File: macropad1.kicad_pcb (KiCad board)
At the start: 2 copper layers, 119.9 x 63.5 mm, 43 parts, among them J1 Conn_01x04, SW1 SW_Reed, SW2 Rotary_Encoder_Switch, U1 ATmega32U4-AU, Y1 16Mhz

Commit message: Ready for prototyping
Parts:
- removed USB1: Molex-0548190589, random-keyboard-parts:Molex-0548190589
- added GND: MountingHole_2.2mm_M2_Pad_Via, MountingHole:MountingHole_2.2mm_M2_Pad_Via, F.Cu at (37.6, 24.1)
- added GND: MountingHole_2.2mm_M2_Pad_Via, MountingHole:MountingHole_2.2mm_M2_Pad_Via, F.Cu at (37.6, 86.4)
- added GND: MountingHole_2.2mm_M2_Pad_Via, MountingHole:MountingHole_2.2mm_M2_Pad_Via, F.Cu at (169.4, 86.4)
- added GND: MountingHole_2.2mm_M2_Pad_Via, MountingHole:MountingHole_2.2mm_M2_Pad_Via, F.Cu at (169.4, 24.1)
- added J2: USB_B_Mini, Connector_USB:USB_Mini-B_Lumberg_2486_01_Horizontal, B.Cu at (65.0, 25.4)
- moved D12 5.18 mm to (165.4, 74.3)
- moved D4 5.18 mm to (165.4, 36.2)
- moved D8 5.18 mm to (165.4, 55.3)
- moved MX12 5.18 mm to (157.5, 74.3)
- moved MX4 5.18 mm to (157.5, 36.2)
- moved MX8 5.18 mm to (157.5, 55.3)
- moved D1 5.18 mm to (108.3, 36.2)
- moved D10 5.18 mm to (127.3, 74.3)
- moved D2 5.18 mm to (127.3, 36.2)
- moved D5 5.18 mm to (108.3, 55.3)
- moved D6 5.18 mm to (127.3, 55.3)
- moved D9 5.18 mm to (108.3, 74.3)
- moved MX1 5.18 mm to (100.3, 36.2)
- moved MX10 5.18 mm to (119.4, 74.3)
- moved MX2 5.18 mm to (119.4, 36.2)
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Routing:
- net /ROW_2: track 106.1 -> 61.8 mm
- net +5V: track 125.5 -> 142.3 mm, vias 2 -> 7
- net GND: track 77.9 -> 64.2 mm, vias 0 -> 2
- net D+: track 55.5 -> 68.2 mm
- net D-: track 58.1 -> 68.7 mm
- net /ROW_1: track 90.1 -> 95.2 mm
- net /COL_0: track 54.0 -> 57.9 mm
- net /ROW_0: track 99.2 -> 102.5 mm
- net /SDA: track 35.0 -> 37.4 mm
- net /SCL: track 33.9 -> 36.3 mm
- net /COL_3: track 115.2 -> 117.4 mm
- net /COL_2: track 93.6 -> 95.9 mm
- net /COL_1: track 75.8 -> 77.9 mm
- net /ENC_S2: track 25.3 -> 26.4 mm
- net /ENC_S1: track 24.6 -> 25.7 mm
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- added copper zone on F.Cu, net (none)
- removed copper zone on F.Cu, net GND
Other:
- board size 119.9 x 63.5 mm -> 139.7 x 69.8 mm
- board text added: "I suppose it's good enough..."

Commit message: Added artwork lib and eeprom
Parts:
- added U2: 24LC512, Package_SO:TSSOP-8_4.4x3mm_P0.65mm, B.Cu at (53.8, 41.9)
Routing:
- net /ROW_2: track 61.8 -> 112.4 mm
- net GND: track 64.2 -> 82.0 mm
- net /SDA: track 37.4 -> 45.1 mm
- net /SCL: track 36.3 -> 43.8 mm
- net +5V: track 142.3 -> 139.7 mm, vias 7 -> 6
- net /COL_2: track 95.9 -> 97.6 mm, vias 0 -> 1
- net /COL_0: track 57.9 -> 57.5 mm, vias 0 -> 1
- net /COL_1: track 77.9 -> 77.8 mm, vias 0 -> 1
- net /COL_3: vias 0 -> 1
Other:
- board text added: "We all gotta start somewhere..."
- board text removed: "I suppose it's good enough..."

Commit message: Added board pics
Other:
- board text added: "JLCJLCJLCJLC"

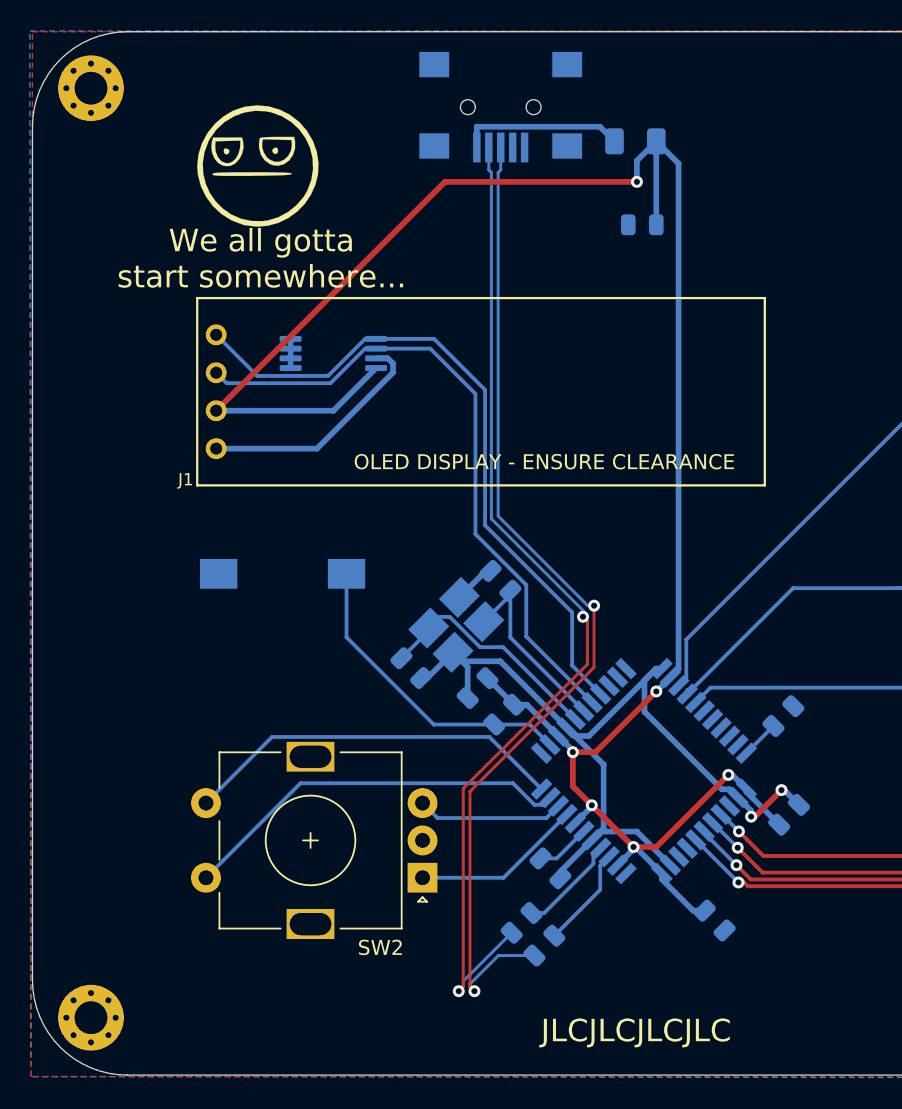
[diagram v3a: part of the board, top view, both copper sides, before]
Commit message: Fixes D+/D- swap and adds ISP header
Also moves some components around for better layout
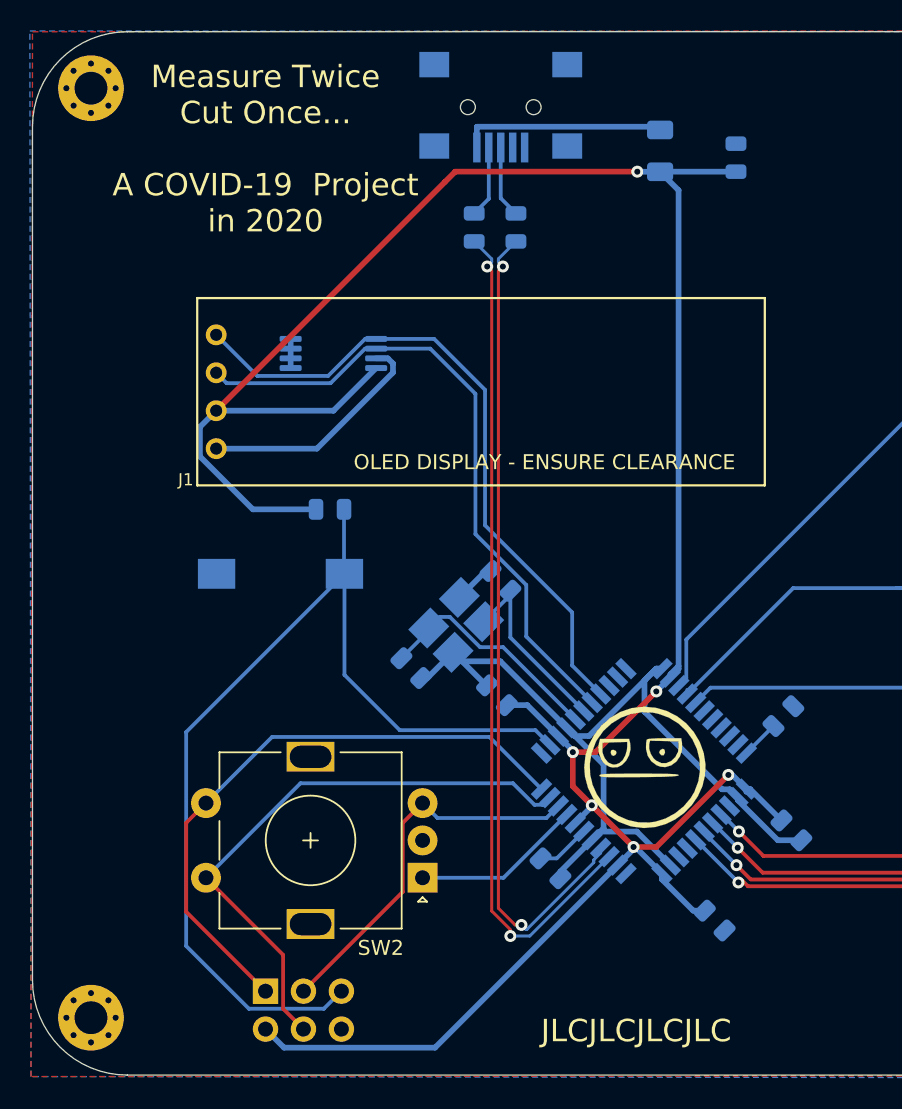
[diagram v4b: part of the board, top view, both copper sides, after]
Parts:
- removed GND (x4): MountingHole_2.2mm_M2_Pad_Via, MountingHole:MountingHole_2.2mm_M2_Pad_Via
- added J3: AVR-ISP-6, Connector_PinHeader_2.54mm:PinHeader_2x03_P2.54mm_Vertical, B.Cu at (49.3, 84.6)
- added REF**: MountingHole_2.2mm_M2_Pad_Via, MountingHole:MountingHole_2.2mm_M2_Pad_Via, F.Cu at (37.6, 86.4)
- added REF**: MountingHole_2.2mm_M2_Pad_Via, MountingHole:MountingHole_2.2mm_M2_Pad_Via, F.Cu at (169.4, 86.4)
- added REF**: MountingHole_2.2mm_M2_Pad_Via, MountingHole:MountingHole_2.2mm_M2_Pad_Via, F.Cu at (169.4, 24.1)
- added REF**: MountingHole_2.2mm_M2_Pad_Via, MountingHole:MountingHole_2.2mm_M2_Pad_Via, F.Cu at (37.6, 24.1)
- SW1: value SW_Reed -> SPST
- moved R3 48.3 mm to (63.2, 33.4), turned to 270 degrees
- moved G*** 47.9 mm to (74.7, 69.6)
- moved R2 46.6 mm to (66.0, 33.4), turned to 90 degrees
- moved R4 18.0 mm to (53.6, 52.3), turned to 0 degrees
- moved C5 7.72 mm to (80.8, 28.8), turned to 90 degrees
- moved F1 1.77 mm to (75.7, 28.3), turned to 90 degrees
- moved C4 1.38 mm to (64.8, 64.8), turned to 135 degrees
- moved C2 1.06 mm to (84.5, 73.8), turned to 315 degrees
- moved SW1 0.14 mm to (50.3, 56.6)
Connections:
- net Net-(R4-Pad2) renamed /!RESET
- J2 pad 2: D+ -> Net-(J2-Pad2)
- J2 pad 3: D- -> Net-(J2-Pad3)
- R2 pad 1: Net-(R2-Pad1) -> D+
- R2 pad 2: D+ -> Net-(J2-Pad3)
- R3 pad 1: Net-(R3-Pad1) -> Net-(J2-Pad2)
- U1 pad 3: Net-(R3-Pad1) -> D-
- U1 pad 4: Net-(R2-Pad1) -> D+
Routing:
- net /!RESET: track 21.0 -> 68.7 mm
- net +5V: track 139.7 -> 176.8 mm
- net /RE_B: track 9.84 -> 25.7 mm
- net /ENC_S1: track 25.7 -> 41.1 mm
- net /ENC_S2: track 26.4 -> 39.3 mm
- net D+: track 68.2 -> 55.3 mm
- net D-: track 68.7 -> 56.6 mm
- net Net-(R2-Pad1): track 7.04 -> 0.00 mm
- net Net-(R3-Pad1): track 6.81 -> 0.00 mm
- net Net-(J2-Pad3): track 0.00 -> 4.83 mm
- net Net-(J2-Pad2): track 0.00 -> 4.82 mm
- net VCC: track 11.0 -> 13.7 mm
- net GND: track 82.0 -> 81.2 mm, vias 2 -> 0
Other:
- board text added: "Measure Twice Cut Once... A COVID-19 Project in 2020"
- board text removed: "We all gotta start somewhere..."

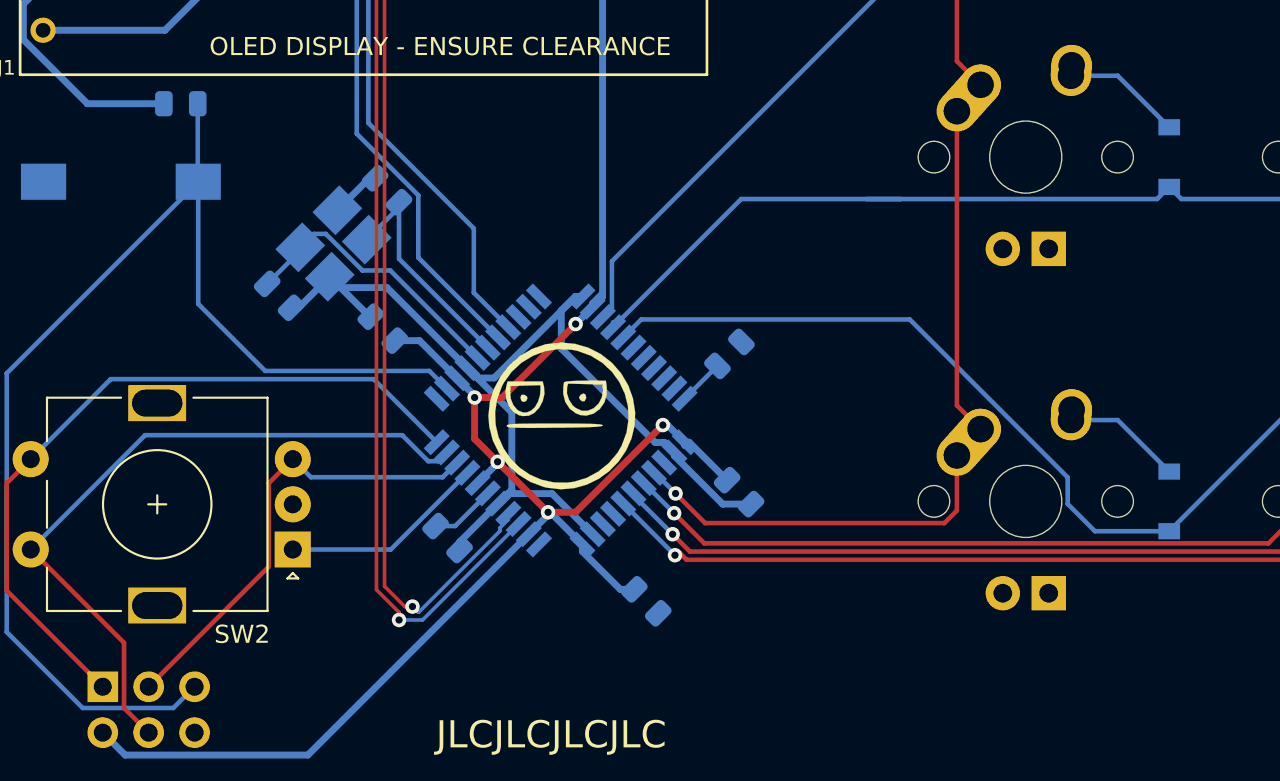
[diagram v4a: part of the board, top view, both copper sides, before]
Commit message: Adds testpads for all unused pins on MCU
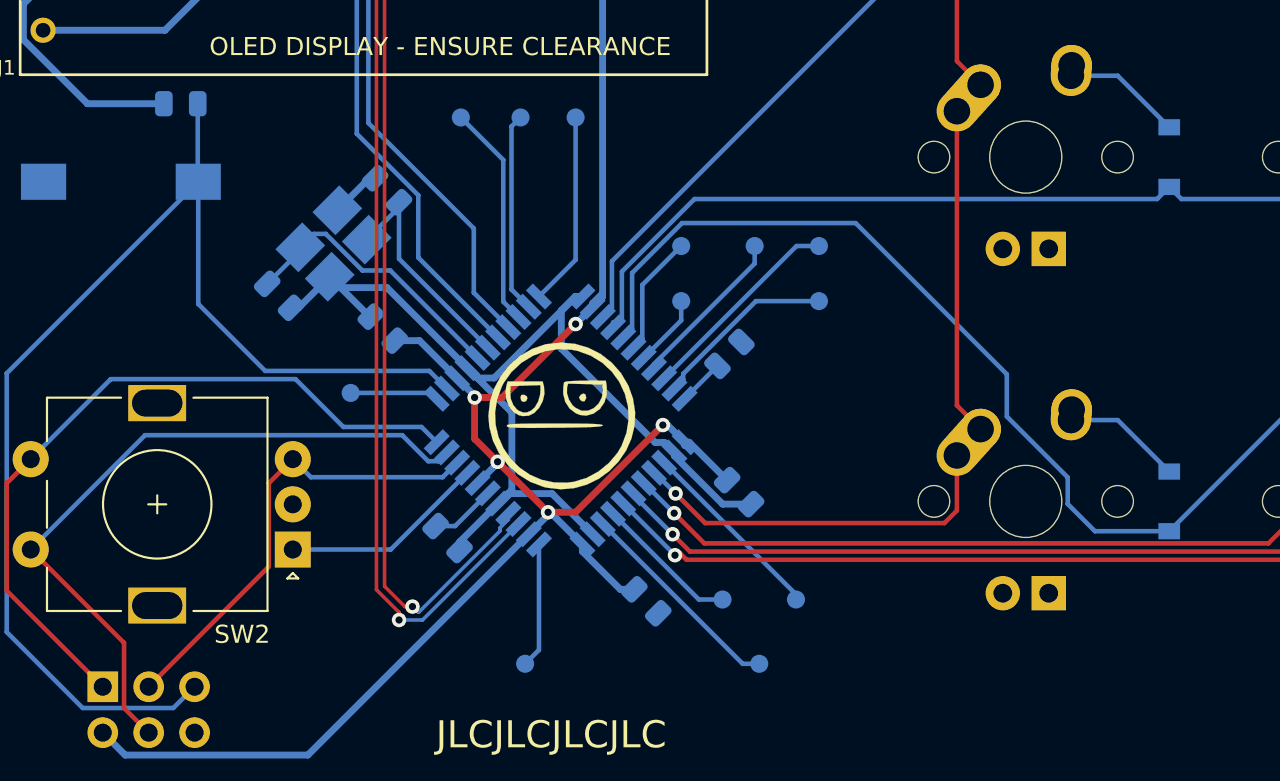
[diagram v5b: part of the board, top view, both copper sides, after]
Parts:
- added P1: TestPoint, TestPoint:TestPoint_Pad_D1.0mm, B.Cu at (72.6, 83.3)
- added P12: TestPoint, TestPoint:TestPoint_Pad_D1.0mm, B.Cu at (63.0, 68.3)
- added P20: TestPoint, TestPoint:TestPoint_Pad_D1.0mm, B.Cu at (69.1, 53.1)
- added P21: TestPoint, TestPoint:TestPoint_Pad_D1.0mm, B.Cu at (72.4, 53.1)
- added P22: TestPoint, TestPoint:TestPoint_Pad_D1.0mm, B.Cu at (75.4, 53.1)
- added P28: TestPoint, TestPoint:TestPoint_Pad_D1.0mm, B.Cu at (81.3, 60.2)
- added P29: TestPoint, TestPoint:TestPoint_Pad_D1.0mm, B.Cu at (81.3, 63.2)
- added P30: TestPoint, TestPoint:TestPoint_Pad_D1.0mm, B.Cu at (85.3, 60.2)
- added P31: TestPoint, TestPoint:TestPoint_Pad_D1.0mm, B.Cu at (88.9, 60.2)
- added P32: TestPoint, TestPoint:TestPoint_Pad_D1.0mm, B.Cu at (88.9, 63.2)
- added P36: TestPoint, TestPoint:TestPoint_Pad_D1.0mm, B.Cu at (87.6, 79.8)
- added P41: TestPoint, TestPoint:TestPoint_Pad_D1.0mm, B.Cu at (83.6, 79.8)
- added P42: TestPoint, TestPoint:TestPoint_Pad_D1.0mm, B.Cu at (85.6, 83.3)
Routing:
- net Net-(P20-Pad1): track 0.00 -> 12.4 mm
- net Net-(P42-Pad1): track 0.00 -> 11.9 mm
- net Net-(P31-Pad1): track 0.00 -> 11.6 mm
- net Net-(P21-Pad1): track 0.00 -> 11.1 mm
- net Net-(P22-Pad1): track 0.00 -> 10.7 mm
- net Net-(P36-Pad1): track 0.00 -> 10.6 mm
- net Net-(P32-Pad1): track 0.00 -> 10.2 mm
- net Net-(P30-Pad1): track 0.00 -> 9.06 mm
- net Net-(P41-Pad1): track 0.00 -> 8.02 mm
- net /ROW_2: track 112.4 -> 120.0 mm
- net Net-(P1-Pad1): track 0.00 -> 6.92 mm
- net Net-(P28-Pad1): track 0.00 -> 6.71 mm
- net Net-(P12-Pad1): track 0.00 -> 4.89 mm
- net Net-(P29-Pad1): track 0.00 -> 4.00 mm

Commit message: Reworks location of traces for ISP header
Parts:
- J3: footprint Connector_PinHeader_2.54mm:PinHeader_2x03_P2.54mm_Vertical -> artwork:ISP-6
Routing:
- net /!RESET: track 68.7 -> 60.2 mm
- net +5V: track 176.8 -> 175.7 mm
